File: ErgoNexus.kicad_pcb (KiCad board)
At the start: 2 copper layers, 162 x 136.5 mm, 110 parts, among them J7 Conn_01x02, J8 Conn_01x02, SW1 SW_Push, SW3 SW_Push, U1 SuperMini nRF52840, U2 SuperMini nRF52840

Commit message: feat: 左側の配線が完了
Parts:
- D_L_11, D_L_12, D_L_13, D_L_14, D_L_15, D_L_16, D_L_21, D_L_22, D_L_23, D_L_24, D_L_25, D_L_26, D_L_31, D_L_32, D_L_33, D_L_34, D_L_35, D_L_36, D_L_41, D_L_42, D_L_43, D_L_44, D_L_45, D_L_46, R5, R6, R7: moved to B.Cu
- moved D_L_46 64.0 mm to (149.7, 174.1)
- moved J8 58.3 mm to (127.2, 164.3), turned to 60 degrees
- moved SW1 49.2 mm to (170.2, 75.1), turned to 0 degrees
- moved D_L_15 47.7 mm to (82.8, 87.1), turned to -6 degrees
- moved K_L_15 45.7 mm to (83.5, 80.8), turned to -6 degrees
- moved RE2 44.9 mm to (143.2, 169.8), turned to -120 degrees
- moved D_L_16 44.3 mm to (62.7, 84.6), turned to 2 degrees
- moved LED1 43.2 mm to (191.2, 119.5), turned to -90 degrees
- moved K_L_16 42.1 mm to (62.6, 78.2), turned to 2 degrees
- moved R7 37.2 mm to (189.7, 115.1), turned to 180 degrees
- moved R6 29.5 mm to (193.2, 115.1)
- moved K_L_26 22.1 mm to (57.6, 99.5), turned to -18.2 degrees
- moved R5 21.9 mm to (193.2, 119.3)
- moved K_L_36 21.1 mm to (49.1, 118.4), turned to -28.75 degrees
- moved D_L_26 20.5 mm to (55.6, 105.2), turned to -18.2 degrees
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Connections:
- U1 pad 10: Col6_L -> Row2_L
- U1 pad 11: unconnected-(U1-P1.04-LF-Pad11) -> Row3_L
- U1 pad 12: Row1_L -> Row4_L
- U1 pad 18: unconnected-(U1-P0.29-LF-Pad18) -> LED_G_L
- U1 pad 19: unconnected-(U1-P0.02-LF-Pad19) -> LED_R_L
- U1 pad 20: unconnected-(U1-P1.15-LF-Pad20) -> LED_B_L
- U1 pad 25: Row2_L -> Col5_L
- U1 pad 26: Row3_L -> Col6_L
- U1 pad 27: Row4_L -> unconnected-(U1-P1.07-LF-Pad27)
- U1 pad 9: Col5_L -> Row1_L
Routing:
- net Col6_L: track 0.00 -> 262.3 mm, vias 0 -> 5
- net Row1_L: track 0.00 -> 200.1 mm, vias 0 -> 2
- net Col5_L: track 0.00 -> 180.4 mm, vias 0 -> 2
- net Col4_L: track 0.00 -> 176.2 mm, vias 0 -> 4
- net GND_L: track 0.00 -> 171.4 mm, vias 0 -> 1
- net Col3_L: track 0.00 -> 161.1 mm, vias 0 -> 4
- net Row4_L: track 0.00 -> 160.8 mm, vias 0 -> 4
- net Row3_L: track 0.00 -> 158.7 mm
- net BAT_L: track 0.00 -> 146.6 mm
- net Row2_L: track 0.00 -> 140.3 mm, vias 0 -> 10
- net Col1_L: track 0.00 -> 135.9 mm, vias 0 -> 2
- net Col2_L: track 19.5 -> 147.2 mm, vias 0 -> 4
- net Ro2_B_L: track 0.00 -> 83.6 mm, vias 0 -> 1
- net Ro2_A_L: track 0.00 -> 78.9 mm, vias 0 -> 1
- net Ro1_A_L: track 0.00 -> 40.0 mm
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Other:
- board size 162 x 136.5 mm -> 341.6 x 136.5 mm

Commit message: fix: キーソケットをGatronLP(KS-33B)用に変更
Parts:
- K_L_11, K_L_12, K_L_13, K_L_14, K_L_15, K_L_16, K_L_21, K_L_22, K_L_23, K_L_24, K_L_25, K_L_26, K_L_31, K_L_32, K_L_33, K_L_34, K_L_35, K_L_36, K_L_41, K_L_42, K_L_43, K_L_44, K_R_11, K_R_12, K_R_13, K_R_14, K_R_15, K_R_16, K_R_21, K_R_22, K_R_23, K_R_24, K_R_25, K_R_26, K_R_31, K_R_32, K_R_33, K_R_34, K_R_35, K_R_36, K_R_41, K_R_42, K_R_43, K_R_44: footprint kbd_SW:CherryMX_Hotswap_1u -> mystster:GatronLP_Hotswap_1u
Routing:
- net Row1_L: track 200.1 -> 132.2 mm, vias 2 -> 10
- net Net-(D_R_25-A): track 13.3 -> 17.1 mm
- net Net-(D_R_43-A): track 12.4 -> 15.8 mm
- net Net-(D_L_23-A): track 13.6 -> 16.8 mm
- net Net-(D_L_32-A): track 12.8 -> 15.9 mm
- net Net-(D_L_33-A): track 12.9 -> 16.0 mm
- net Net-(D_L_43-A): track 12.8 -> 15.7 mm
- net Net-(D_R_36-A): track 12.8 -> 15.7 mm
- net Net-(D_R_13-A): track 13.6 -> 16.5 mm
- net Net-(D_L_25-A): track 12.9 -> 15.8 mm
- net Net-(D_L_36-A): track 13.1 -> 15.8 mm
- net Net-(D_L_26-A): track 12.5 -> 15.1 mm
- net Net-(D_R_34-A): track 14.5 -> 17.1 mm
- net Net-(D_L_34-A): track 14.5 -> 17.1 mm
- net Net-(D_L_35-A): track 13.0 -> 15.6 mm
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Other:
- board size 341.6 x 136.5 mm -> 342 x 136.5 mm

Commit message: feat: add mouse bites
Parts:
- added Ref**: Val**, kbd_Hole:Mouse_Bite_Hole, F.Cu at (360.4, 120.8)
- added Ref**: Val**, kbd_Hole:Mouse_Bite_Hole, F.Cu at (198.5, 126.0)
- added Ref**: Val**, kbd_Hole:Mouse_Bite_Hole, F.Cu at (34.8, 120.8)
- added Ref**: Val**, kbd_Hole:Mouse_Bite_Hole, F.Cu at (166.9, 194.8)
- added Ref**: Val**, kbd_Hole:Mouse_Bite_Hole, F.Cu at (106.9, 57.9)
- added Ref**: Val**, kbd_Hole:Mouse_Bite_Hole, F.Cu at (198.5, 166.2)
- added Ref**: Val**, kbd_Hole:Mouse_Bite_Hole, F.Cu at (196.9, 87.5)
- added Ref**: Val**, kbd_Hole:Mouse_Bite_Hole, F.Cu at (228.2, 194.8)
- added Ref**: Val**, kbd_Hole:Mouse_Bite_Hole, F.Cu at (196.9, 126.0)
- added Ref**: Val**, kbd_Hole:Mouse_Bite_Hole, F.Cu at (362.8, 54.0)
- added Ref**: Val**, kbd_Hole:Mouse_Bite_Hole, F.Cu at (196.9, 166.2)
- added Ref**: Val**, kbd_Hole:Mouse_Bite_Hole, F.Cu at (198.5, 87.5)
- added Ref**: Val**, kbd_Hole:Mouse_Bite_Hole, F.Cu at (288.0, 57.9)
- moved J7 18.6 mm to (265.6, 164.7)
- moved D_R_31 16.0 mm to (246.7, 134.3)
- moved D_R_43 16.0 mm to (250.2, 155.3)
- moved K_R_22 16.0 mm to (255.5, 98.0)
- moved K_R_31 16.0 mm to (244.3, 128.7)
- moved D_R_11 16.0 mm to (235.2, 96.1)
- moved D_R_12 16.0 mm to (253.2, 84.6)
- moved D_R_13 16.0 mm to (271.7, 76.1)
- moved D_R_14 16.0 mm to (292.1, 80.6)
- moved D_R_15 16.0 mm to (312.5, 87.1)
- moved D_R_16 16.0 mm to (332.7, 84.6)
- moved D_R_21 16.0 mm to (239.7, 115.6)
- moved D_R_22 16.0 mm to (256.7, 104.1)
- moved D_R_23 16.0 mm to (274.7, 96.2)
- moved D_R_24 16.0 mm to (295.7, 100.1)
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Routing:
- net Net-(D_L_24-A): track 13.2 -> 16.3 mm
- net Row3_L: track 158.7 -> 159.8 mm
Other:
- board size 342 x 136.5 mm -> 340.4 x 150.5 mm

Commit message: feat: add tooling holes and fiducials
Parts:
- removed Ref** (x13): Val**, kbd_Hole:Mouse_Bite_Hole
- added REF**: mouse-bite-4.2mm, mystster:mouse-bite-4.2mm, F.Cu at (106.9, 57.9)
- added REF**: mouse-bite-5.1mm, mystster:mouse-bite-5.1mm, F.Cu at (362.7, 53.8)
- added REF**: mouse-bite-4.2mm, mystster:mouse-bite-4.2mm, F.Cu at (198.5, 87.5)
- added REF**: mouse-bite-5.1mm, mystster:mouse-bite-5.1mm, F.Cu at (362.7, 199.0)
- added REF**: MountingHole_2.1mm, MountingHole:MountingHole_2.1mm, F.Cu at (365.4, 196.6)
- added REF**: mouse-bite-4.2mm, mystster:mouse-bite-4.2mm, F.Cu at (166.9, 194.7)
- added REF**: mouse-bite-4.2mm, mystster:mouse-bite-4.2mm, F.Cu at (196.9, 126.0)
- added REF**: mouse-bite-5.1mm, mystster:mouse-bite-5.1mm, F.Cu at (32.7, 198.9)
- added REF**: MountingHole_2.1mm, MountingHole:MountingHole_2.1mm, F.Cu at (30.0, 56.1)
- added REF**: hole-1mm, mystster:hole-1mm, F.Cu at (365.4, 193.0)
- added REF**: mouse-bite-4.2mm, mystster:mouse-bite-4.2mm, F.Cu at (360.4, 120.7)
- added REF**: mouse-bite-4.2mm, mystster:mouse-bite-4.2mm, F.Cu at (196.9, 87.5)
- added REF**: mouse-bite-4.2mm, mystster:mouse-bite-4.2mm, F.Cu at (34.9, 120.7)
- added REF**: hole-1mm, mystster:hole-1mm, F.Cu at (365.4, 59.8)
- added REF**: MountingHole_2.1mm, MountingHole:MountingHole_2.1mm, F.Cu at (365.4, 56.2)
- added REF**: mouse-bite-4.2mm, mystster:mouse-bite-4.2mm, F.Cu at (288.0, 57.9)
- added REF**: MountingHole_2.1mm, MountingHole:MountingHole_2.1mm, F.Cu at (30.1, 196.6)
- added REF**: mouse-bite-5.1mm, mystster:mouse-bite-5.1mm, F.Cu at (32.8, 53.8)
- added REF**: mouse-bite-4.2mm, mystster:mouse-bite-4.2mm, F.Cu at (196.9, 166.2)
- added REF**: hole-1mm, mystster:hole-1mm, F.Cu at (30.0, 193.0)
- added REF**: hole-1mm, mystster:hole-1mm, F.Cu at (30.0, 59.8)
- added REF**: mouse-bite-4.2mm, mystster:mouse-bite-4.2mm, F.Cu at (198.5, 126.0)
- added REF**: mouse-bite-4.2mm, mystster:mouse-bite-4.2mm, F.Cu at (228.2, 194.7)
- added REF**: mouse-bite-4.2mm, mystster:mouse-bite-4.2mm, F.Cu at (198.5, 166.2)

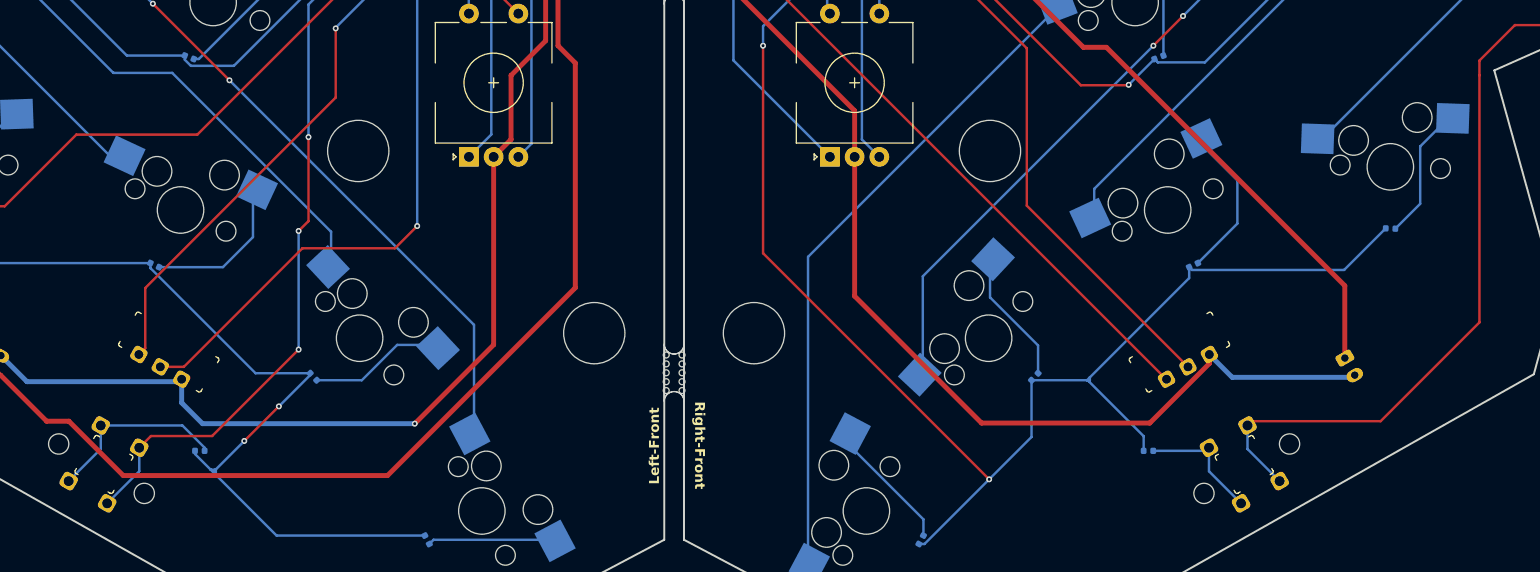
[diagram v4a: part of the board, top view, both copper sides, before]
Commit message: feat: 水平ロータリーエンコーダのスイッチ部品を変更
元々の11mmだと高すぎるのでエンコーダを7mmに変更。
それに伴い、switchも高さの低いものに変更する必要があり、フットプリントを変更
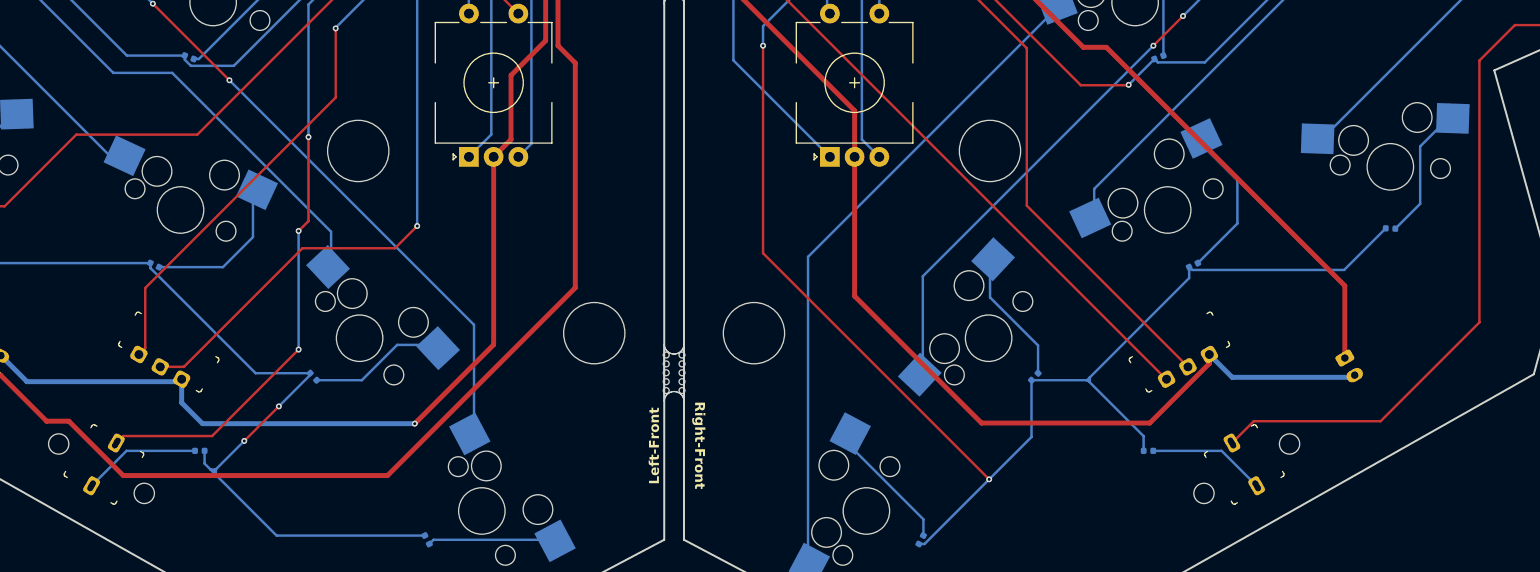
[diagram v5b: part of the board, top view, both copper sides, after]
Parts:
- RE2, RE4: footprint THQWGD001:THQWGD001C [4pin] #1 -> THQWGD001:THQWGD001C [2pin] #1
- turned D_L_46 to 180 degrees
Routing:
- net K_L_46_out: track 18.7 -> 11.9 mm
- net Col6_L: track 262.3 -> 257.4 mm
- net Col6_R: track 297.7 -> 293.1 mm
- net K_R_46_out: track 12.7 -> 11.9 mm

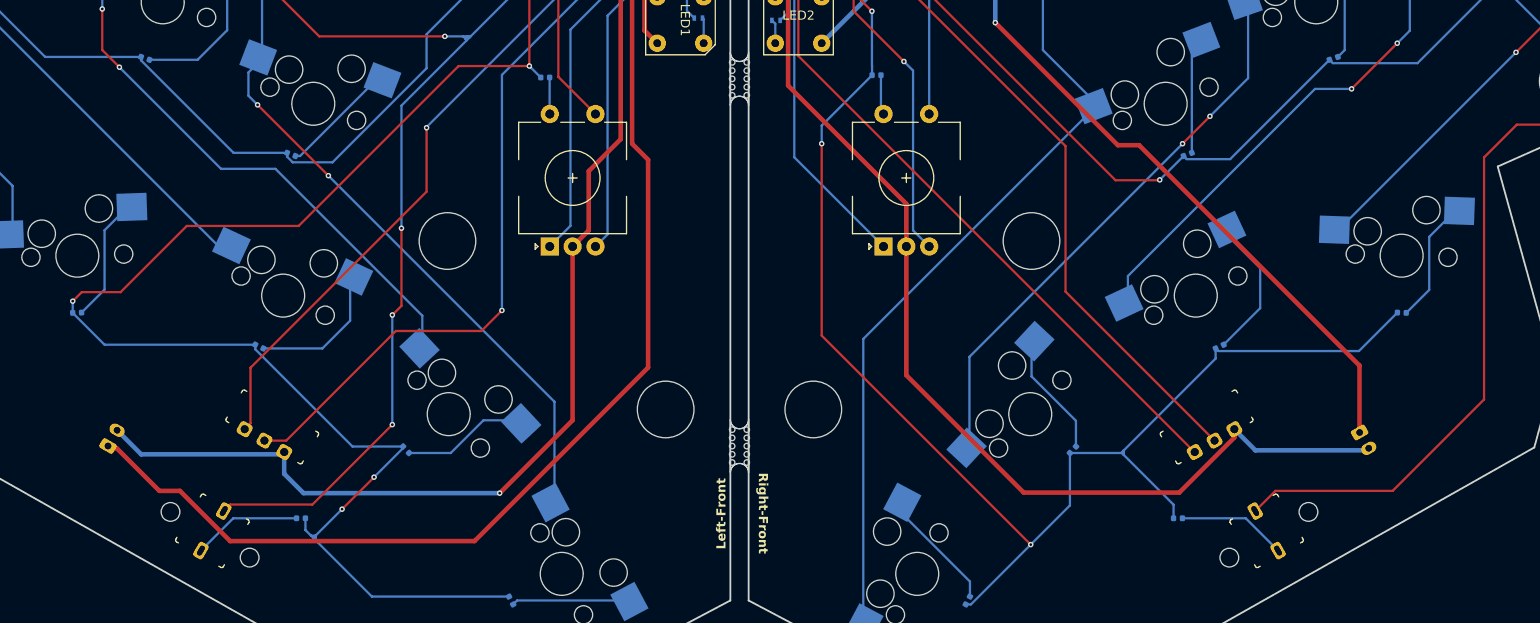
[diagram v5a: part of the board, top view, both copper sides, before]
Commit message: feat: change rotary encoder position
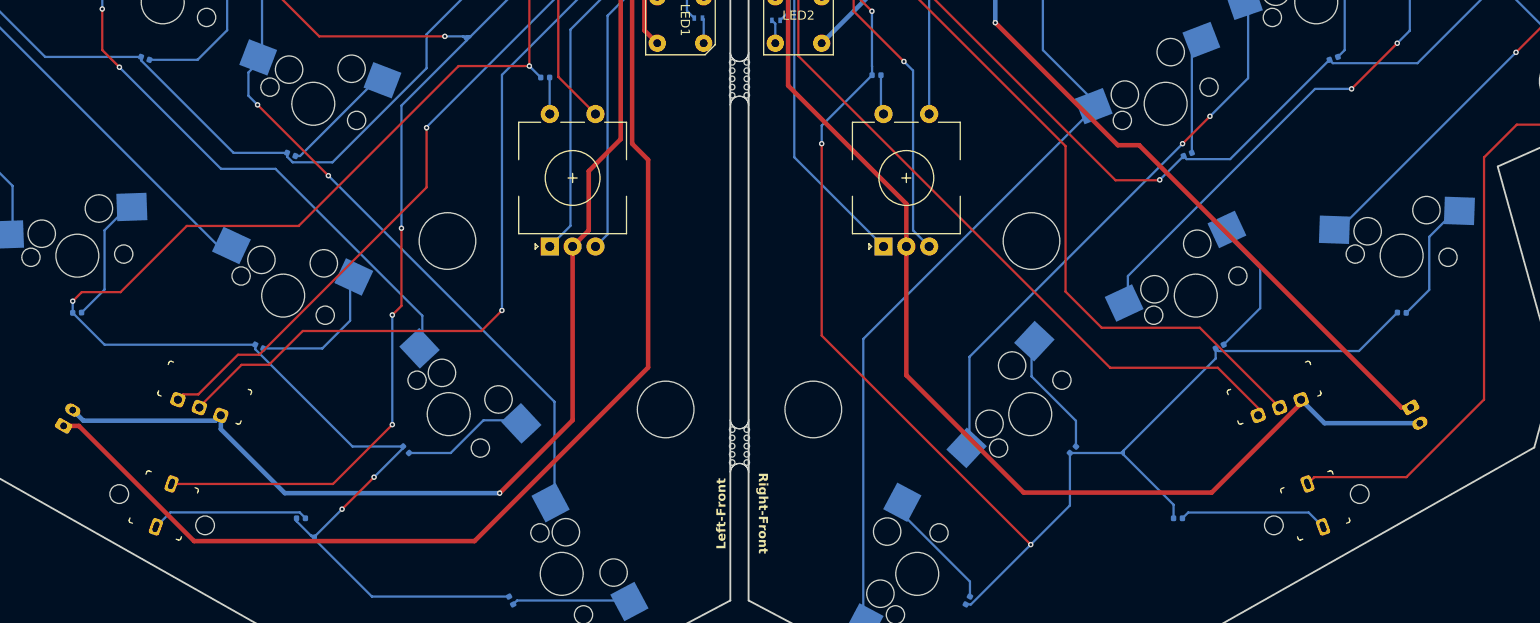
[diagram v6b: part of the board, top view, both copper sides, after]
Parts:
- moved RE2 7.14 mm to (136.9, 166.6), turned to -110 degrees
- moved RE4 7.14 mm to (258.5, 166.6), turned to -70 degrees
- moved J7 6.24 mm to (271.2, 161.9)
- moved J8 5.33 mm to (123.7, 164.0)
- turned D_L_46 to 0 degrees
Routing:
- net Col6_R: track 293.1 -> 286.1 mm
- net GND_R: track 173.5 -> 180.2 mm
- net BAT_L: track 146.6 -> 152.7 mm
- net GND_L: track 171.4 -> 177.3 mm
- net Ro2_A_R: track 80.7 -> 86.4 mm
- net Ro2_B_L: track 83.6 -> 89.3 mm
- net Ro2_B_R: track 79.9 -> 85.5 mm
- net K_L_46_out: track 11.9 -> 17.3 mm
- net Col6_L: track 257.4 -> 261.9 mm
- net K_R_46_out: track 11.9 -> 16.3 mm
- net Ro2_A_L: track 78.9 -> 81.1 mm

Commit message: feat: 親指キーを少し上に変更
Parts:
- RE2, RE4: footprint THQWGD001:THQWGD001C [2pin] #1 -> THQWGD001:THQWGD001C [2pin] #2
- RE3: value RotaryEncoder_Switch -> RotaryEncoder
- moved REF** 2.59 mm to (169.5, 194.7)
- moved REF** 2.21 mm to (226.0, 194.7)
- moved D_L_41 1.05 mm to (172.7, 182.0)
- moved D_L_42 1.05 mm to (161.2, 165.5)
- moved D_L_43 1.05 mm to (145.1, 154.2)
- moved D_L_44 1.05 mm to (125.2, 150.5)
- moved D_L_46 1.05 mm to (149.7, 173.0)
- moved D_R_41 1.05 mm to (222.7, 182.0)
- moved D_R_42 1.05 mm to (234.2, 165.5)
- moved D_R_43 1.05 mm to (250.2, 154.2)
- moved D_R_44 1.05 mm to (270.2, 150.5)
- moved D_R_46 1.05 mm to (245.7, 173.0)
- moved K_L_41 1.05 mm to (178.2, 179.1)
- moved K_L_42 1.05 mm to (165.9, 161.6)
- moved K_L_43 1.05 mm to (147.7, 148.7)
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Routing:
- net Ro2_A_R: track 86.4 -> 97.4 mm, vias 0 -> 1
- net Ro2_B_L: track 89.3 -> 79.0 mm
- net Row4_L: track 160.8 -> 151.1 mm
- net GND_L: track 177.3 -> 186.4 mm, vias 1 -> 0
- net Col6_L: track 261.9 -> 254.4 mm, vias 5 -> 4
- net Ro2_A_L: track 81.1 -> 74.3 mm
- net BAT_L: track 152.7 -> 146.2 mm
- net GND_R: track 180.2 -> 186.6 mm
- net Net-(D_R_43-A): track 15.8 -> 12.4 mm
- net Ro2_B_R: track 85.5 -> 82.9 mm
- net K_L_46_out: track 17.3 -> 19.2 mm
- net Net-(D_R_42-A): track 13.2 -> 12.2 mm
- net Row4_R: track 154.8 -> 155.8 mm
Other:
- outline, holes or cut-outs redrawn

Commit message: fix: ルールチェックエラーの修正
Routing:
- net Col4_R: track 155.5 -> 158.5 mm
- net Col3_L: track 161.1 -> 158.4 mm
- net Net-(D_R_41-A): track 13.1 -> 11.5 mm
- net Col1_R: track 121.2 -> 119.9 mm
- net Net-(D_R_25-A): track 17.1 -> 16.1 mm
- net Col4_L: track 176.2 -> 175.2 mm
- net Net-(D_L_13-A): track 15.3 -> 14.4 mm
- net Net-(D_L_23-A): track 16.8 -> 16.0 mm
- net Net-(D_R_31-A): track 12.5 -> 11.6 mm
- net Net-(D_L_24-A): track 16.3 -> 15.4 mm
- net Net-(D_R_32-A): track 13.2 -> 12.4 mm
- net Net-(D_R_33-A): track 12.4 -> 11.6 mm
- net Col3_R: track 152.7 -> 152.0 mm
- net Col2_R: track 135.1 -> 134.4 mm
- net Net-(D_L_44-A): track 13.6 -> 13.1 mm
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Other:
- outline, holes or cut-outs redrawn
